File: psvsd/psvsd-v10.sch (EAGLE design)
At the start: 30 parts, among them J1 MEM2051-00-195-00, U1 USB2244QFN, U3 VREG, Y1 24.000MHz

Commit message: Removed old LDO and reset circuit. Added new power efficient POR circuit & dual channel LDO
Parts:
- added C16: 1uF, rcl:C-EUC0603
- added C17: 1nF, rcl:C-EUC0402
- added C18: 0.1uF, resistor:C-EUC0402
- added C19: 0.1uF, rcl:C-EUC0402
- added D1: 3.3V, diode:DIODE-SOD523
- added U2: 74AUP1G74DC, NXP_60_26022015:74AUP1G74DC
- C2: value 10uF -> 1uF
- R2: value 165K -> 100K
- U3: value VREG -> LP3996_DSC_10; device v-reg-micrel:MIC5219XX -> LP3996:LP3996_DSC_10
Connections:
- net VDD18PLL renamed USBVDD18PLL
- new net N$2: C19.1, D1.A, R3.1, U2-G.!S
- new net N$4: C17.1, U3.CBYP
- new net N$5: C18.1, U3.SET
- new net ONSWA: U$1G$1.ONSWA, U2-G.C
- new net PSHOLD: U$1G$1.PSHOLD, U2-G.!Q, U2-G.D, U3.EN2
- new net USBVDD18: C8.1, U1.VDD18
- net !RESET: now also U3.POR; no longer R3.2
- net GND: now also C16.2, C17.2, C18.2, C19.2, U2-P.GND, U3.DAP; no longer R2.1
- net VDD18: now also C16.1, D1.C, R3.2, U2-G.!R, U2-P.VCC, U3.OUT1; no longer C8.1, U1.VDD18
- net VDD33: now also R2.1, U3.OUT2; no longer U3.OUT
- net VDD5: now also U3.EN1; no longer R3.1, U3.EN

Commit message: Layout for PM circuit
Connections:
- net N$2 renamed !S
- net N$4 renamed CBYP
- net N$5 renamed CSET
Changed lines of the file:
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@@
 <?xml version="1.0" encoding="utf-8"?>
 <!DOCTYPE eagle SYSTEM "eagle.dtd">
-<eagle version="8.2.0">
+<eagle version="8.2.2">
 <drawing>
 <settings>
@@
 </segment>
 </net>
-<net name="N$4" class="0">
+<net name="CBYP" class="0">
 <segment>
 <pinref part="U3" gate="A" pin="CBYP"/>
@@
 </segment>
 </net>
-<net name="N$5" class="0">
+<net name="CSET" class="0">
 <segment>
 <pinref part="U3" gate="A" pin="SET"/>
@@
 </segment>
 </net>
-<net name="N$2" class="0">
+<net name="!S" class="0">
 <segment>
 <pinref part="R3" gate="G$1" pin="1"/>

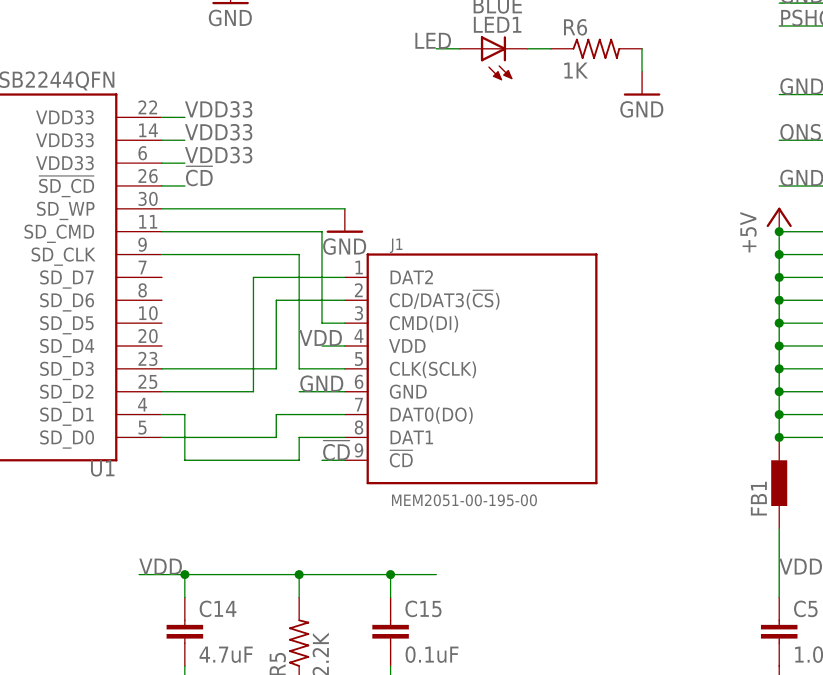
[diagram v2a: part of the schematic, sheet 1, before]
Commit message: Changed to cheaper molex slot
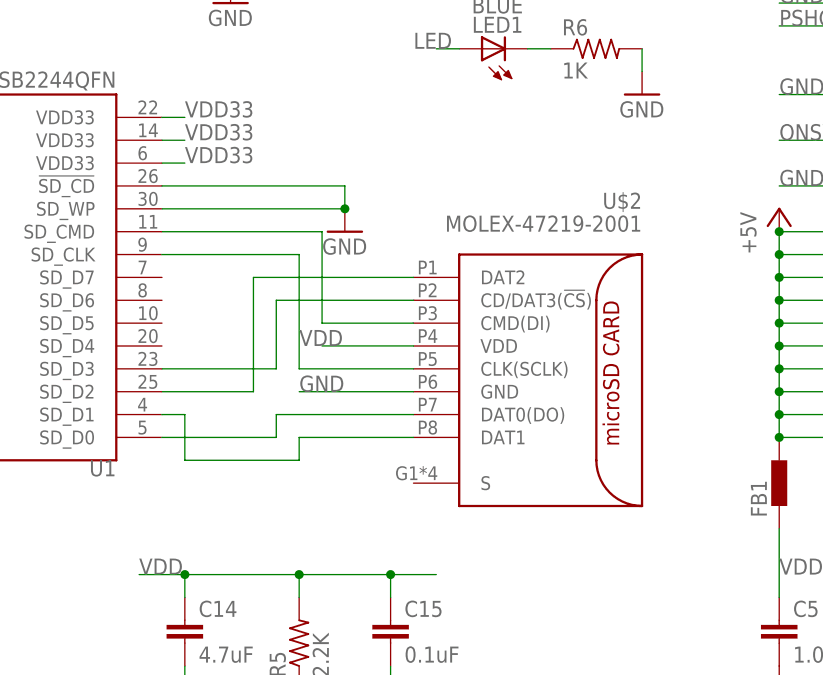
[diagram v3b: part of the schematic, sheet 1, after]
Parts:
- removed J1: MEM2051-00-195-00, sd-mmc:MEM2051-00-195-00
- added U$2: MOLEX-47219-2001, molex:MOLEX-47219-2001
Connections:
- removed net !CD: J1.!CD, U1.!SD_CD
- net GND: now also U$2.GND, U1.!SD_CD; no longer J1.GND
- net SD_CLK: now also U$2.CLK(SCLK); no longer J1.CLK(SCLK)
- net SD_CMD: now also U$2.CMD(DI); no longer J1.CMD(DI)
- net SD_D0: now also U$2.DAT0(DO); no longer J1.DAT0(DO)
- net SD_D1: now also U$2.DAT1; no longer J1.DAT1
- net SD_D2: now also U$2.DAT2; no longer J1.DAT2
- net SD_D3: now also U$2.CD/DAT3(!CS!); no longer J1.CD/DAT3(!CS!)
- net VDD: now also U$2.VDD; no longer J1.VDD
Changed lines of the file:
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@@
 <part name="GND" library="supply1" deviceset="GND" device=""/>
 <part name="P+1" library="supply1" deviceset="+5V" device=""/>
-<part name="J1" library="sd-mmc" deviceset="MEM2051" device="-00-195-00"/>
 <part name="U1" library="USB2244" deviceset="USB2244" device="QFN"/>
 <part name="JP1" library="pinhead" deviceset="PINHD-1X5" device="" value="UART_KERMIT"/>
@@
 <part name="GND18" library="supply1" library_urn="urn:adsk.eagle:library:371" deviceset="GND" device=""/>
 <part name="C17" library="rcl" library_urn="urn:adsk.eagle:library:334" deviceset="C-EU" device="C0402" value="1nF"/>
+<part name="U$2" library="molex" deviceset="MOLEX-47219-2001" device=""/>
 </parts>
 <sheets>
@@
 <instance part="GND" gate="1" x="55.88" y="-30.48"/>
 <instance part="P+1" gate="1" x="-45.72" y="-2.54"/>
-<instance part="J1" gate="G$1" x="-78.74" y="-17.78"/>
 <instance part="U1" gate="G$1" x="-132.08" y="-10.16" rot="R180"/>
 <instance part="JP1" gate="A" x="68.58" y="22.86"/>
@@
 <instance part="R6" gate="G$1" x="-66.04" y="15.24"/>
 <instance part="GND15" gate="1" x="-60.96" y="10.16"/>
+<instance part="U$2" gate="G$1" x="-78.74" y="-20.32" rot="MR0"/>
 </instances>
 <busses>
@@
 </segment>
 <segment>
-<pinref part="J1" gate="G$1" pin="GND"/>
-<wire x1="-93.98" y1="-22.86" x2="-99.06" y2="-22.86" width="0.1524" layer="91"/>
 <label x="-99.06" y="-22.86" size="1.778" layer="95"/>
+<pinref part="U$2" gate="G$1" pin="GND"/>
+<wire x1="-99.06" y1="-22.86" x2="-86.36" y2="-22.86" width="0.1524" layer="91"/>
 </segment>
 <segment>
@@
 <wire x1="-114.3" y1="-2.54" x2="-93.98" y2="-2.54" width="0.1524" layer="91"/>
 <pinref part="GND13" gate="1" pin="GND"/>
+<pinref part="U1" gate="G$1" pin="!SD_CD"/>
+<wire x1="-114.3" y1="0" x2="-93.98" y2="0" width="0.1524" layer="91"/>
+<wire x1="-93.98" y1="0" x2="-93.98" y2="-2.54" width="0.1524" layer="91"/>
+<junction x="-93.98" y="-2.54"/>
 </segment>
 <segment>
@@
 <net name="SD_D0" class="0">
 <segment>
-<pinref part="J1" gate="G$1" pin="DAT0(DO)"/>
-<wire x1="-93.98" y1="-25.4" x2="-101.6" y2="-25.4" width="0.1524" layer="91"/>
 <wire x1="-101.6" y1="-25.4" x2="-101.6" y2="-27.94" width="0.1524" layer="91"/>
 <pinref part="U1" gate="G$1" pin="SD_D0"/>
 <wire x1="-101.6" y1="-27.94" x2="-114.3" y2="-27.94" width="0.1524" layer="91"/>
+<pinref part="U$2" gate="G$1" pin="DAT0(DO)"/>
+<wire x1="-101.6" y1="-25.4" x2="-86.36" y2="-25.4" width="0.1524" layer="91"/>
 </segment>
 </net>
 <net name="SD_D1" class="0">
 <segment>
-<pinref part="J1" gate="G$1" pin="DAT1"/>
-<wire x1="-93.98" y1="-27.94" x2="-99.06" y2="-27.94" width="0.1524" layer="91"/>
 <wire x1="-99.06" y1="-27.94" x2="-99.06" y2="-30.48" width="0.1524" layer="91"/>
 <wire x1="-99.06" y1="-30.48" x2="-111.76" y2="-30.48" width="0.1524" layer="91"/>
@@
 <pinref part="U1" gate="G$1" pin="SD_D1"/>
 <wire x1="-111.76" y1="-25.4" x2="-114.3" y2="-25.4" width="0.1524" layer="91"/>
+<pinref part="U$2" gate="G$1" pin="DAT1"/>
+<wire x1="-86.36" y1="-27.94" x2="-99.06" y2="-27.94" width="0.1524" layer="91"/>
 </segment>
 </net>
 <net name="SD_D2" class="0">
 <segment>
-<pinref part="J1" gate="G$1" pin="DAT2"/>
-<wire x1="-93.98" y1="-10.16" x2="-104.14" y2="-10.16" width="0.1524" layer="91"/>
 <wire x1="-104.14" y1="-10.16" x2="-104.14" y2="-22.86" width="0.1524" layer="91"/>
 <pinref part="U1" gate="G$1" pin="SD_D2"/>
 <wire x1="-104.14" y1="-22.86" x2="-114.3" y2="-22.86" width="0.1524" layer="91"/>
+<pinref part="U$2" gate="G$1" pin="DAT2"/>
+<wire x1="-104.14" y1="-10.16" x2="-86.36" y2="-10.16" width="0.1524" layer="91"/>
 </segment>
 </net>
 <net name="SD_D3" class="0">
 <segment>
-<pinref part="J1" gate="G$1" pin="CD/DAT3(!CS!)"/>
-<wire x1="-93.98" y1="-12.7" x2="-101.6" y2="-12.7" width="0.1524" layer="91"/>
 <wire x1="-101.6" y1="-12.7" x2="-101.6" y2="-20.32" width="0.1524" layer="91"/>
 <pinref part="U1" gate="G$1" pin="SD_D3"/>
 <wire x1="-101.6" y1="-20.32" x2="-114.3" y2="-20.32" width="0.1524" layer="91"/>
+<pinref part="U$2" gate="G$1" pin="CD/DAT3(!CS!)"/>
+<wire x1="-101.6" y1="-12.7" x2="-86.36" y2="-12.7" width="0.1524" layer="91"/>
 </segment>
 </net>
 <net name="SD_CMD" class="0">
 <segment>
-<pinref part="J1" gate="G$1" pin="CMD(DI)"/>
-<wire x1="-93.98" y1="-15.24" x2="-96.52" y2="-15.24" width="0.1524" layer="91"/>
 <wire x1="-96.52" y1="-15.24" x2="-96.52" y2="-5.08" width="0.1524" layer="91"/>
 <pinref part="U1" gate="G$1" pin="SD_CMD"/>
 <wire x1="-96.52" y1="-5.08" x2="-114.3" y2="-5.08" width="0.1524" layer="91"/>
+<pinref part="U$2" gate="G$1" pin="CMD(DI)"/>
+<wire x1="-96.52" y1="-15.24" x2="-86.36" y2="-15.24" width="0.1524" layer="91"/>
 </segment>
 </net>
 <net name="SD_CLK" class="0">
 <segment>
-<pinref part="J1" gate="G$1" pin="CLK(SCLK)"/>
-<wire x1="-93.98" y1="-20.32" x2="-99.06" y2="-20.32" width="0.1524" layer="91"/>
 <wire x1="-99.06" y1="-20.32" x2="-99.06" y2="-7.62" width="0.1524" layer="91"/>
 <pinref part="U1" gate="G$1" pin="SD_CLK"/>
 <wire x1="-99.06" y1="-7.62" x2="-114.3" y2="-7.62" width="0.1524" layer="91"/>
+<pinref part="U$2" gate="G$1" pin="CLK(SCLK)"/>
+<wire x1="-99.06" y1="-20.32" x2="-86.36" y2="-20.32" width="0.1524" layer="91"/>
 </segment>
 </net>
@@
 <net name="VDD" class="0">
 <segment>
-<pinref part="J1" gate="G$1" pin="VDD"/>
-<wire x1="-93.98" y1="-17.78" x2="-96.52" y2="-17.78" width="0.1524" layer="91"/>
 <label x="-99.06" y="-17.78" size="1.778" layer="95"/>
+<pinref part="U$2" gate="G$1" pin="VDD"/>
+<wire x1="-96.52" y1="-17.78" x2="-86.36" y2="-17.78" width="0.1524" layer="91"/>
 </segment>
 <segment>
@@
 </segment>
 </net>
-<net name="!CD" class="0">
-<segment>
-<pinref part="U1" gate="G$1" pin="!SD_CD"/>
-<wire x1="-114.3" y1="0" x2="-111.76" y2="0" width="0.1524" layer="91"/>
-<label x="-111.76" y="0" size="1.778" layer="95"/>
-</segment>
-<segment>
-<pinref part="J1" gate="G$1" pin="!CD"/>
-<wire x1="-93.98" y1="-30.48" x2="-96.52" y2="-30.48" width="0.1524" layer="91"/>
-<label x="-96.52" y="-30.48" size="1.778" layer="95"/>
-</segment>
-</net>

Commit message: Placed labels for new components
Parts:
- renumbered U$2 to SD1
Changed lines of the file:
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@@
 <part name="GND18" library="supply1" library_urn="urn:adsk.eagle:library:371" deviceset="GND" device=""/>
 <part name="C17" library="rcl" library_urn="urn:adsk.eagle:library:334" deviceset="C-EU" device="C0402" value="1nF"/>
-<part name="U$2" library="molex" deviceset="MOLEX-47219-2001" device=""/>
+<part name="SD1" library="molex" deviceset="MOLEX-47219-2001" device=""/>
 </parts>
 <sheets>
@@
 <instance part="R6" gate="G$1" x="-66.04" y="15.24"/>
 <instance part="GND15" gate="1" x="-60.96" y="10.16"/>
-<instance part="U$2" gate="G$1" x="-78.74" y="-20.32" rot="MR0"/>
+<instance part="SD1" gate="G$1" x="-78.74" y="-20.32" rot="MR0"/>
 </instances>
 <busses>
@@
 <segment>
 <label x="-99.06" y="-22.86" size="1.778" layer="95"/>
-<pinref part="U$2" gate="G$1" pin="GND"/>
+<pinref part="SD1" gate="G$1" pin="GND"/>
 <wire x1="-99.06" y1="-22.86" x2="-86.36" y2="-22.86" width="0.1524" layer="91"/>
 </segment>
@@
 <pinref part="U1" gate="G$1" pin="SD_D0"/>
 <wire x1="-101.6" y1="-27.94" x2="-114.3" y2="-27.94" width="0.1524" layer="91"/>
-<pinref part="U$2" gate="G$1" pin="DAT0(DO)"/>
+<pinref part="SD1" gate="G$1" pin="DAT0(DO)"/>
 <wire x1="-101.6" y1="-25.4" x2="-86.36" y2="-25.4" width="0.1524" layer="91"/>
 </segment>
@@
 <pinref part="U1" gate="G$1" pin="SD_D1"/>
 <wire x1="-111.76" y1="-25.4" x2="-114.3" y2="-25.4" width="0.1524" layer="91"/>
-<pinref part="U$2" gate="G$1" pin="DAT1"/>
+<pinref part="SD1" gate="G$1" pin="DAT1"/>
 <wire x1="-86.36" y1="-27.94" x2="-99.06" y2="-27.94" width="0.1524" layer="91"/>
 </segment>
@@
 <pinref part="U1" gate="G$1" pin="SD_D2"/>
 <wire x1="-104.14" y1="-22.86" x2="-114.3" y2="-22.86" width="0.1524" layer="91"/>
-<pinref part="U$2" gate="G$1" pin="DAT2"/>
+<pinref part="SD1" gate="G$1" pin="DAT2"/>
 <wire x1="-104.14" y1="-10.16" x2="-86.36" y2="-10.16" width="0.1524" layer="91"/>
 </segment>
@@
 <pinref part="U1" gate="G$1" pin="SD_D3"/>
 <wire x1="-101.6" y1="-20.32" x2="-114.3" y2="-20.32" width="0.1524" layer="91"/>
-<pinref part="U$2" gate="G$1" pin="CD/DAT3(!CS!)"/>
+<pinref part="SD1" gate="G$1" pin="CD/DAT3(!CS!)"/>
 <wire x1="-101.6" y1="-12.7" x2="-86.36" y2="-12.7" width="0.1524" layer="91"/>
 </segment>
@@
 <pinref part="U1" gate="G$1" pin="SD_CMD"/>
 <wire x1="-96.52" y1="-5.08" x2="-114.3" y2="-5.08" width="0.1524" layer="91"/>
-<pinref part="U$2" gate="G$1" pin="CMD(DI)"/>
+<pinref part="SD1" gate="G$1" pin="CMD(DI)"/>
 <wire x1="-96.52" y1="-15.24" x2="-86.36" y2="-15.24" width="0.1524" layer="91"/>
 </segment>
@@
 <pinref part="U1" gate="G$1" pin="SD_CLK"/>
 <wire x1="-99.06" y1="-7.62" x2="-114.3" y2="-7.62" width="0.1524" layer="91"/>
-<pinref part="U$2" gate="G$1" pin="CLK(SCLK)"/>
+<pinref part="SD1" gate="G$1" pin="CLK(SCLK)"/>
 <wire x1="-99.06" y1="-20.32" x2="-86.36" y2="-20.32" width="0.1524" layer="91"/>
 </segment>
@@
 <segment>
 <label x="-99.06" y="-17.78" size="1.778" layer="95"/>
-<pinref part="U$2" gate="G$1" pin="VDD"/>
+<pinref part="SD1" gate="G$1" pin="VDD"/>
 <wire x1="-96.52" y1="-17.78" x2="-86.36" y2="-17.78" width="0.1524" layer="91"/>
 </segment>

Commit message: Changed crystal
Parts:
- Y1: device crystal:CRYSTALCTS406 -> crystal:XRCGB
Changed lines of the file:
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@@
 <layer number="54" name="bGND_GNDA" color="1" fill="9" visible="no" active="no"/>
 <layer number="56" name="wert" color="7" fill="1" visible="no" active="no"/>
+<layer number="57" name="tCAD" color="11" fill="1" visible="no" active="no"/>
+<layer number="58" name="bCAD" color="11" fill="1" visible="no" active="no"/>
 <layer number="90" name="Modules" color="5" fill="1" visible="yes" active="yes"/>
 <layer number="91" name="Nets" color="2" fill="1" visible="yes" active="yes"/>
@@
 <part name="GND1" library="supply1" deviceset="GND" device=""/>
 <part name="C2" library="rcl" deviceset="C-EU" device="C0603" value="1uF"/>
-<part name="Y1" library="crystal" deviceset="CRYSTAL" device="CTS406" value="24.000MHz"/>
+<part name="Y1" library="crystal" deviceset="XRCGB" device="" value="24.000MHz"/>
 <part name="R1" library="rcl" deviceset="R-US_" device="R0603" value="1M"/>
 <part name="C3" library="rcl" deviceset="C-EU" device="C0402" value="18pF"/>
